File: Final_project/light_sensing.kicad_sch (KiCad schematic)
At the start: 0 parts

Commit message: Add miniproj parts, begin photosensing circuit
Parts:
- added C?: C, symbol Device:C
- added D?: D_Photo, symbol Device:D_Photo
- added R?: R, symbol Device:R
- added U?: MCP6021T-E_OT, Package_TO_SOT_SMD:SOT-23-5, symbol miniproject:MCP6021T-E_OT
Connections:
- new net: C?.1, D?.1 (K), R?.1, U?.4 (-)
- new net +3V3: U?.2 (V+)
- new net GND: D?.2 (A), U?.3 (+), U?.5 (V-)
- new net Vout_photo: C?.2, R?.2, U?.1
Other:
- note added: "Capacitor Cf is used to prevent oscillation or gain peaking and to set the output bandwidth (1/2πRC)"
- note added: "Pick out parts for - photodiode - capacitor - resistor"
- note added: "RC filter"
- note added: "Vout = Ip*Rƒ"
- note added: "proportional to the light intensity characteristics of the photodiode"
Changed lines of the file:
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@@
 (kicad_sch (version 20211123) (generator eeschema)
-  (paper "A4")
+  (paper "A5")
+  (junction (at 90.17 48.26) (diameter 0) (color 0 0 0 0)
+  )
+  (junction (at 54.61 69.85) (diameter 0) (color 0 0 0 0)
+  )
+  (junction (at 54.61 48.26) (diameter 0) (color 0 0 0 0)
+  )
+  (junction (at 54.61 74.93) (diameter 0) (color 0 0 0 0)
+  )
+  (junction (at 90.17 63.5) (diameter 0) (color 0 0 0 0)
+  )
+  (junction (at 54.61 58.42) (diameter 0) (color 0 0 0 0)
+  )
+  (wire (pts (xy 90.17 38.1) (xy 90.17 48.26))
+    (stroke (width 0) (type default) (color 0 0 0 0))
+  )
+  (wire (pts (xy 54.61 69.85) (xy 69.85 69.85))
+    (stroke (width 0) (type default) (color 0 0 0 0))
+  )
+  (wire (pts (xy 90.17 48.26) (xy 90.17 63.5))
+    (stroke (width 0) (type default) (color 0 0 0 0))
+  )
+  (wire (pts (xy 71.12 38.1) (xy 54.61 38.1))
+    (stroke (width 0) (type default) (color 0 0 0 0))
+  )
+  (wire (pts (xy 71.12 48.26) (xy 54.61 48.26))
+    (stroke (width 0) (type default) (color 0 0 0 0))
+  )
+  (wire (pts (xy 54.61 48.26) (xy 54.61 58.42))
+    (stroke (width 0) (type default) (color 0 0 0 0))
+  )
+  (wire (pts (xy 74.93 54.61) (xy 74.93 55.88))
+    (stroke (width 0) (type default) (color 0 0 0 0))
+  )
+  (wire (pts (xy 90.17 63.5) (xy 95.25 63.5))
+    (stroke (width 0) (type default) (color 0 0 0 0))
+  )
+  (wire (pts (xy 78.74 48.26) (xy 90.17 48.26))
+    (stroke (width 0) (type default) (color 0 0 0 0))
+  )
+  (wire (pts (xy 85.09 63.5) (xy 90.17 63.5))
+    (stroke (width 0) (type default) (color 0 0 0 0))
+  )
+  (wire (pts (xy 54.61 58.42) (xy 54.61 59.69))
+    (stroke (width 0) (type default) (color 0 0 0 0))
+  )
+  (wire (pts (xy 78.74 38.1) (xy 90.17 38.1))
+    (stroke (width 0) (type default) (color 0 0 0 0))
+  )
+  (wire (pts (xy 74.93 74.93) (xy 54.61 74.93))
+    (stroke (width 0) (type default) (color 0 0 0 0))
+  )
+  (wire (pts (xy 54.61 58.42) (xy 69.85 58.42))
+    (stroke (width 0) (type default) (color 0 0 0 0))
+  )
+  (wire (pts (xy 54.61 69.85) (xy 54.61 74.93))
+    (stroke (width 0) (type default) (color 0 0 0 0))
+  )
+  (wire (pts (xy 74.93 71.12) (xy 74.93 74.93))
+    (stroke (width 0) (type default) (color 0 0 0 0))
+  )
+  (wire (pts (xy 54.61 74.93) (xy 54.61 81.28))
+    (stroke (width 0) (type default) (color 0 0 0 0))
+  )
+  (wire (pts (xy 69.85 58.42) (xy 69.85 60.96))
+    (stroke (width 0) (type default) (color 0 0 0 0))
+  )
+  (wire (pts (xy 69.85 69.85) (xy 69.85 66.04))
+    (stroke (width 0) (type default) (color 0 0 0 0))
+  )
+  (wire (pts (xy 54.61 67.31) (xy 54.61 69.85))
+    (stroke (width 0) (type default) (color 0 0 0 0))
+  )
+  (wire (pts (xy 54.61 38.1) (xy 54.61 48.26))
+    (stroke (width 0) (type default) (color 0 0 0 0))
+  )
+  (text "Vout = Ip*Rƒ" (at 16.51 20.32 0)
+    (effects (font (size 1.27 1.27)) (justify left bottom))
+  )
+  (text "Pick out parts for\n- photodiode\n- capacitor\n- resistor"
+    (at 21.59 53.34 0)
+    (effects (font (size 1.27 1.27)) (justify left bottom))
+  )
+  (text "proportional to the light intensity characteristics of the photodiode"
+    (at 16.51 22.86 0)
+    (effects (font (size 1.27 1.27)) (justify left bottom))
+  )
+  (text "Capacitor Cf is used to prevent oscillation or gain peaking and to set the output bandwidth (1/2πRC)"
+    (at 16.51 25.4 0)
+    (effects (font (size 1.27 1.27)) (justify left bottom))
+  )
+  (text "RC filter" (at 109.22 21.59 0)
+    (effects (font (size 1.27 1.27)) (justify left bottom))
+  )
+  (hierarchical_label "Vout_photo" (shape output) (at 95.25 63.5 0)
+    (effects (font (size 1.27 1.27)) (justify left))
+  )
+  (symbol (lib_id "Device:R") (at 74.93 48.26 90) (unit 1)
+    (in_bom yes) (on_board yes) (fields_autoplaced)
+    (property "Reference" "R?" (id 0) (at 74.93 41.91 90))
+    (property "Value" "R" (id 1) (at 74.93 44.45 90))
+    (property "Footprint" "" (id 2) (at 74.93 50.038 90)
+      (effects (font (size 1.27 1.27)) hide)
+    )
+    (property "Datasheet" "~" (id 3) (at 74.93 48.26 0)
+      (effects (font (size 1.27 1.27)) hide)
+    )
+    (pin "1")
+    (pin "2")
+  )
+  (symbol (lib_id "miniproject:MCP6021T-E_OT") (at 77.47 63.5 0) (unit 1)
+    (in_bom yes) (on_board yes)
+    (property "Reference" "U?" (id 0) (at 78.74 68.58 0))
+    (property "Value" "MCP6021T-E_OT" (id 1) (at 85.09 71.12 0))
+    (property "Footprint" "Package_TO_SOT_SMD:SOT-23-5" (id 2) (at 77.47 63.5 0)
+      (effects (font (size 1.27 1.27)) hide)
+    )
+    (property "Datasheet" "https://ww1.microchip.com/downloads/en/DeviceDoc/20001685E.pdf" (id 3) (at 77.47 58.42 0)
+      (effects (font (size 1.27 1.27)) hide)
+    )
+    (pin "2")
+    (pin "5")
+    (pin "1")
+    (pin "3")
+    (pin "4")
+  )
+  (symbol (lib_id "Device:D_Photo") (at 54.61 64.77 270) (unit 1)
+    (in_bom yes) (on_board yes) (fields_autoplaced)
+    (property "Reference" "D?" (id 0) (at 59.69 62.5474 90)
+      (effects (font (size 1.27 1.27)) (justify left))
+    )
+    (property "Value" "D_Photo" (id 1) (at 59.69 65.0874 90)
+      (effects (font (size 1.27 1.27)) (justify left))
+    )
+    (property "Footprint" "" (id 2) (at 54.61 63.5 0)
+      (effects (font (size 1.27 1.27)) hide)
+    )
+    (property "Datasheet" "~" (id 3) (at 54.61 63.5 0)
+      (effects (font (size 1.27 1.27)) hide)
+    )
+    (pin "1")
+    (pin "2")
+  )
+  (symbol (lib_id "power:GND") (at 54.61 81.28 0) (unit 1)
+    (in_bom yes) (on_board yes) (fields_autoplaced)
+    (property "Reference" "#PWR?" (id 0) (at 54.61 87.63 0)
+      (effects (font (size 1.27 1.27)) hide)
+    )
+    (property "Value" "GND" (id 1) (at 54.61 86.36 0))
+    (property "Footprint" "" (id 2) (at 54.61 81.28 0)
+      (effects (font (size 1.27 1.27)) hide)
+    )
+    (property "Datasheet" "" (id 3) (at 54.61 81.28 0)
+      (effects (font (size 1.27 1.27)) hide)
+    )
+    (pin "1")
+  )
+  (symbol (lib_id "Device:C") (at 74.93 38.1 90) (unit 1)
+    (in_bom yes) (on_board yes) (fields_autoplaced)
+    (property "Reference" "C?" (id 0) (at 74.93 30.48 90))
+    (property "Value" "C" (id 1) (at 74.93 33.02 90))
+    (property "Footprint" "" (id 2) (at 78.74 37.1348 0)
+      (effects (font (size 1.27 1.27)) hide)
+    )
+    (property "Datasheet" "~" (id 3) (at 74.93 38.1 0)
+      (effects (font (size 1.27 1.27)) hide)
+    )
+    (pin "1")
+    (pin "2")
+  )
+  (symbol (lib_id "power:+3V3") (at 74.93 54.61 0) (unit 1)
+    (in_bom yes) (on_board yes) (fields_autoplaced)
+    (property "Reference" "#PWR?" (id 0) (at 74.93 58.42 0)
+      (effects (font (size 1.27 1.27)) hide)
+    )
+    (property "Value" "+3V3" (id 1) (at 77.47 53.3399 0)
+      (effects (font (size 1.27 1.27)) (justify left))
+    )
+    (property "Footprint" "" (id 2) (at 74.93 54.61 0)
+      (effects (font (size 1.27 1.27)) hide)
+    )
+    (property "Datasheet" "" (id 3) (at 74.93 54.61 0)
+      (effects (font (size 1.27 1.27)) hide)
+    )
+    (pin "1")
+  )
 )

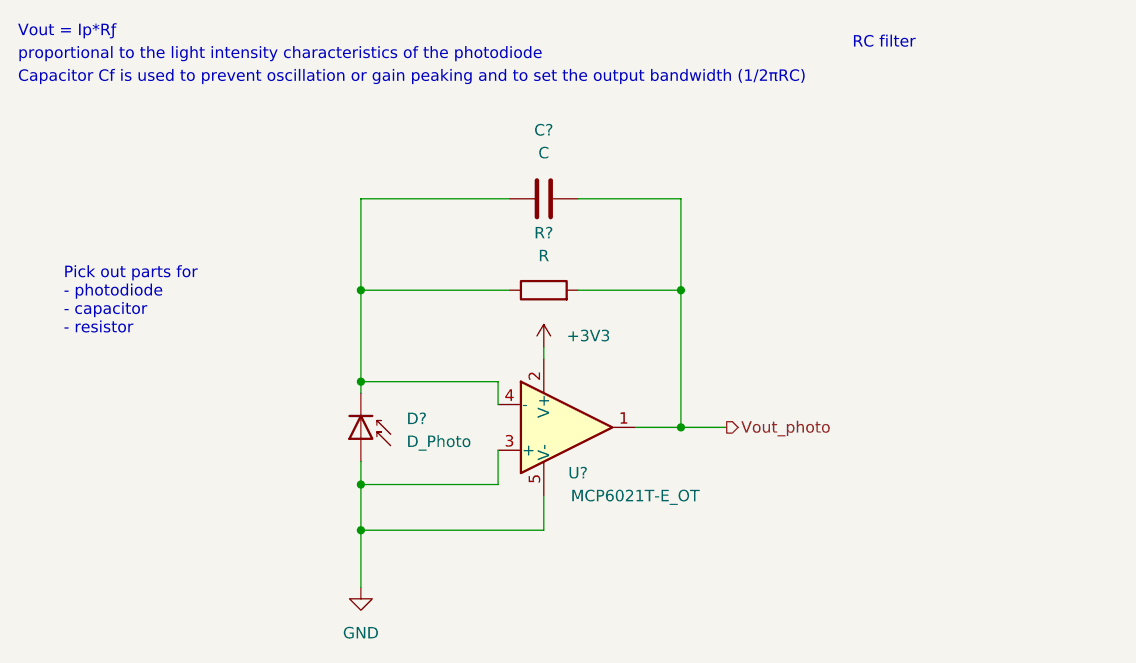
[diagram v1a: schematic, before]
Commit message: added copy of light sensing module
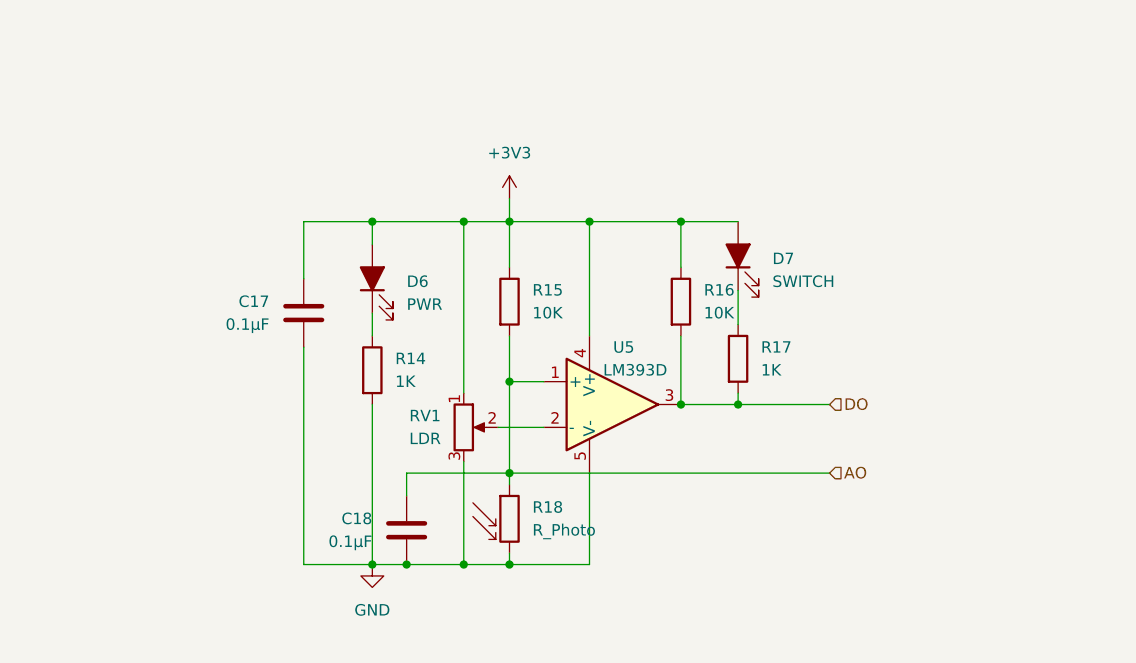
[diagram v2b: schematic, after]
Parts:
- removed C?: C, symbol Device:C
- removed D?: D_Photo, symbol Device:D_Photo
- removed R?: R, symbol Device:R
- removed U?: MCP6021T-E_OT, Package_TO_SOT_SMD:SOT-23-5, symbol miniproject:MCP6021T-E_OT
- added C17, C18: 0.1µF, Final_project:CL10B104JB8NNNC, symbol Device:C
- added D6: PWR, Final_project:LTST-C170TGKT, symbol Device:LED_Filled
- added D7: SWITCH, Final_project:LTST-C170TGKT, symbol Device:LED_Filled
- added R14, R17: 1K, Final_project:RC0603FR-071KL, symbol Device:R
- added R15, R16: 10K, Resistor_SMD:R_0805_2012Metric, symbol Device:R
- added R18: R_Photo, Final_project:02-LDR4, symbol Device:R_Photo
- added RV1: LDR, Final_project:TRIM_T73YU103KT20, symbol Device:R_Potentiometer
- added U5: LM393D, Final_project:LM393D, symbol pspice:OPAMP
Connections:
- net +3V3: now also C17.2, D6.2 (A), D7.2 (A), R15.1, R16.1, RV1.1, U5.4 (V+)
- net GND: now also C17.1, C18.1, R14.2, R18.2, RV1.3, U5.5 (V-)
- new net: RV1.2, U5.2 (-)
- new net: D6.1 (K), R14.1
- new net: D7.1 (K), R17.1
- new net AO: C18.2, R15.2, R18.1, U5.1 (+)
- new net DO: R16.2, R17.2, U5.3
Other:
- note removed: "Capacitor Cf is used to prevent oscillation or gain peaking and to set the output bandwidth (1/2πRC)"
- note removed: "Pick out parts for - photodiode - capacitor - resistor"
- note removed: "RC filter"
- note removed: "Vout = Ip*Rƒ"
- note removed: "proportional to the light intensity characteristics of the photodiode"

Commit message: Add 3d, fixing vias and layout issues
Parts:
- C17, C18: footprint Final_project:CL10B104JB8NNNC -> Capacitor_SMD:C_0603_1608Metric; Digi-Key_Part (none) -> CL10B104JB8NNNC
- R14, R17: footprint Final_project:RC0603FR-071KL -> Resistor_SMD:R_0603_1608Metric; Digi-Key_Part (none) -> RC0603FR-071KL
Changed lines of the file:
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@@
       (effects (font (size 1.27 1.27)) (justify right))
     )
-    (property "Footprint" "Final_project:CL10B104JB8NNNC" (id 2) (at 60.6552 71.12 0)
+    (property "Footprint" "Capacitor_SMD:C_0603_1608Metric" (id 2) (at 60.6552 71.12 0)
       (effects (font (size 1.27 1.27)) hide)
     )
@@
       (effects (font (size 1.27 1.27)) hide)
     )
+    (property "Digi-Key_Part" "CL10B104JB8NNNC" (id 4) (at 59.69 74.93 0)
+      (effects (font (size 1.27 1.27)) hide)
+    )
     (pin "1")
     (pin "2")
@@
       (effects (font (size 1.27 1.27)) hide)
     )
-    (property "Datasheet" "https://www.yageo.com/upload/media/product/productsearch/datasheet/rchip/PYu-RC_Group_51_RoHS_L_12.pdf" (id 3) (at 71.12 49.53 0)
+    (property "Datasheet" "~" (id 3) (at 71.12 49.53 0)
       (effects (font (size 1.27 1.27)) hide)
     )
@@
       (effects (font (size 1.27 1.27)) hide)
     )
-    (property "Datasheet" "https://www.yageo.com/upload/media/product/productsearch/datasheet/rchip/PYu-RC_Group_51_RoHS_L_12.pdf" (id 3) (at 90.17 49.53 0)
+    (property "Datasheet" "~" (id 3) (at 90.17 49.53 0)
       (effects (font (size 1.27 1.27)) hide)
     )
@@
       (effects (font (size 1.27 1.27)) (justify left))
     )
-    (property "Footprint" "Final_project:RC0603FR-071KL" (id 2) (at 54.102 57.15 90)
-      (effects (font (size 1.27 1.27)) hide)
-    )
-    (property "Datasheet" "~" (id 3) (at 55.88 57.15 0)
+    (property "Footprint" "Resistor_SMD:R_0603_1608Metric" (id 2) (at 54.102 57.15 90)
+      (effects (font (size 1.27 1.27)) hide)
+    )
+    (property "Datasheet" "https://www.yageo.com/upload/media/product/productsearch/datasheet/rchip/PYu-RC_Group_51_RoHS_L_12.pdf" (id 3) (at 55.88 57.15 0)
+      (effects (font (size 1.27 1.27)) hide)
+    )
+    (property "Digi-Key_Part" "RC0603FR-071KL" (id 4) (at 55.88 57.15 0)
       (effects (font (size 1.27 1.27)) hide)
     )
@@
       (effects (font (size 1.27 1.27)) (justify left))
     )
-    (property "Footprint" "Final_project:RC0603FR-071KL" (id 2) (at 94.742 55.88 90)
-      (effects (font (size 1.27 1.27)) hide)
-    )
-    (property "Datasheet" "~" (id 3) (at 96.52 55.88 0)
+    (property "Footprint" "Resistor_SMD:R_0603_1608Metric" (id 2) (at 94.742 55.88 90)
+      (effects (font (size 1.27 1.27)) hide)
+    )
+    (property "Datasheet" "https://www.yageo.com/upload/media/product/productsearch/datasheet/rchip/PYu-RC_Group_51_RoHS_L_12.pdf" (id 3) (at 96.52 55.88 0)
+      (effects (font (size 1.27 1.27)) hide)
+    )
+    (property "Digi-Key_Part" "RC0603FR-071KL" (id 4) (at 96.52 55.88 0)
       (effects (font (size 1.27 1.27)) hide)
     )
@@
       (effects (font (size 1.27 1.27)) (justify right))
     )
-    (property "Footprint" "Final_project:CL10B104JB8NNNC" (id 2) (at 49.2252 46.99 0)
+    (property "Footprint" "Capacitor_SMD:C_0603_1608Metric" (id 2) (at 49.2252 46.99 0)
       (effects (font (size 1.27 1.27)) hide)
     )
@@
       (effects (font (size 1.27 1.27)) hide)
     )
+    (property "Digi-Key_Part" "CL10B104JB8NNNC" (id 4) (at 48.26 50.8 0)
+      (effects (font (size 1.27 1.27)) hide)
+    )
